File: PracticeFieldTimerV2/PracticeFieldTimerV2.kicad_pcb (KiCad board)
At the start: 2 copper layers, 103 x 96 mm, 36 parts, among them J1 External Controls, J2 Screw_Terminal_01x04, J3 Panel, J5 /CAN Enable, J6 RJ45-B, J7 RJ45-A, U1 ESP32-DevKitC, U4 DS3231MZ_TRL, U5 SN65HVD230DR

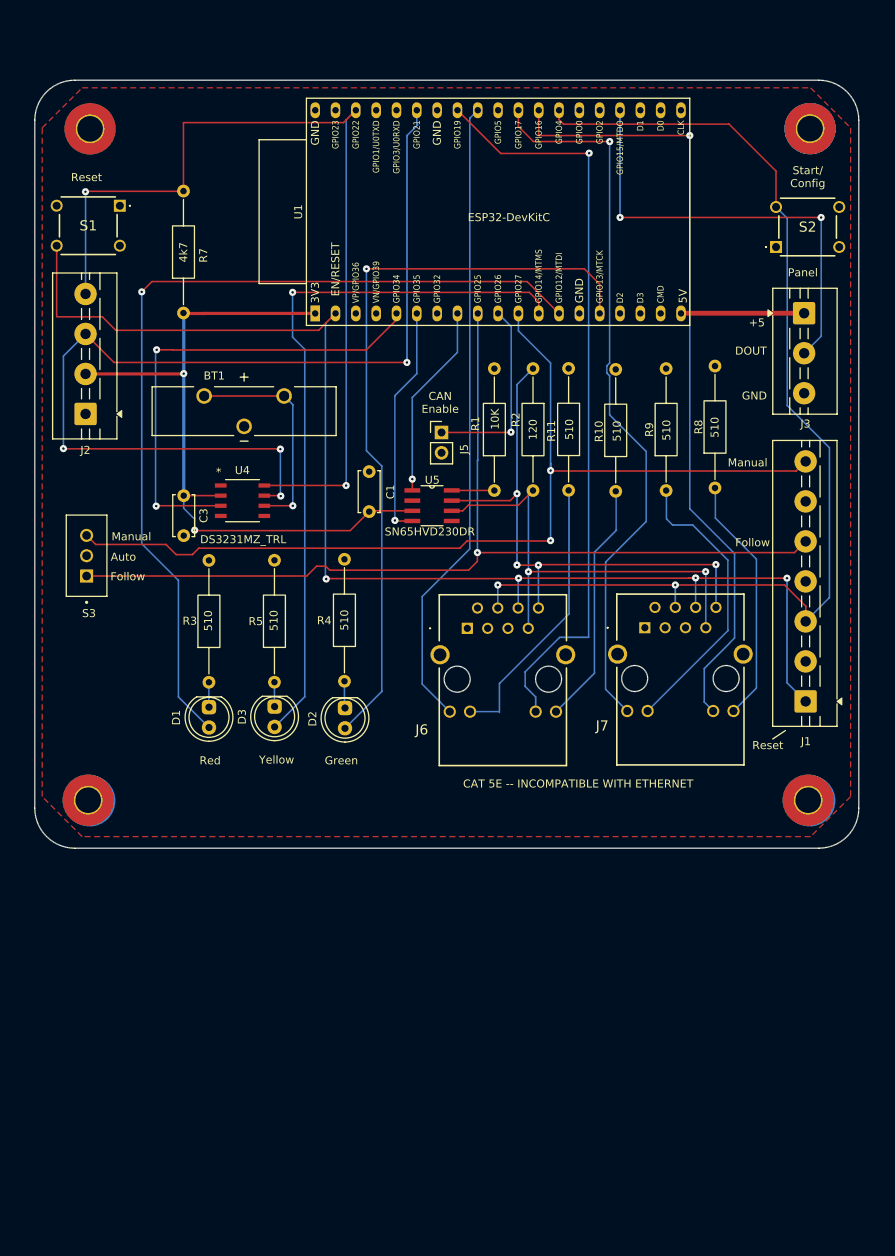
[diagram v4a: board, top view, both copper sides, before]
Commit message: Add missing resistors. Fix the warnings we can. Cosmetic fixes. Getting close
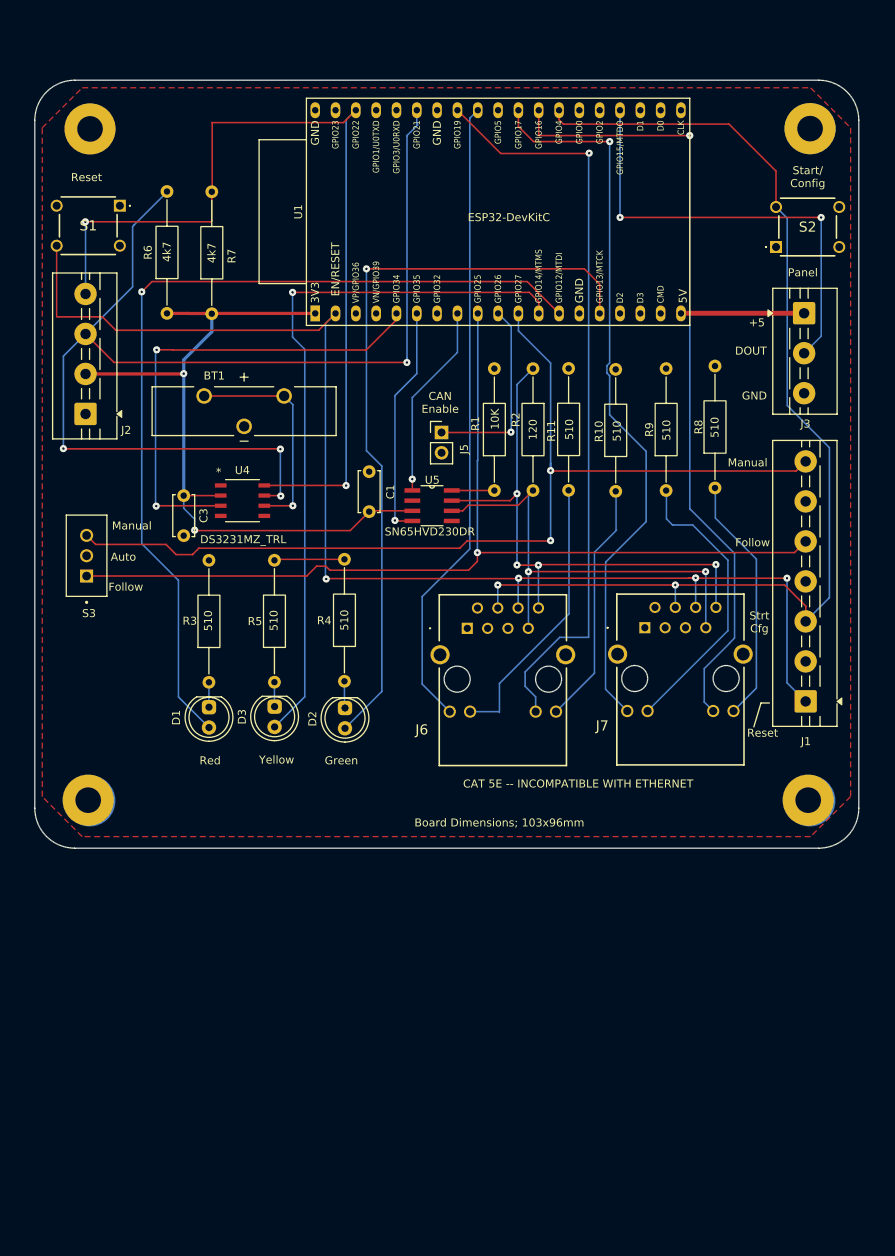
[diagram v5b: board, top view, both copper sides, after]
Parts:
- added R6: 4k7, Resistor_THT:R_Axial_DIN0207_L6.3mm_D2.5mm_P15.24mm_Horizontal, F.Cu at (57.0, 60.1)
- moved R7 3.54 mm to (62.6, 60.2)
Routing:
- net I2C SDA: track 124.4 -> 146.3 mm
- net GND: track 0.92 -> 9.72 mm
- net +3.3V: track 89.3 -> 92.7 mm
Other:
- board text added: "Board Dimensions; 103x96mm"
- board text added: "Strt Cfg"

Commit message: Smush components closer together to reduce width under 100 mm because cost of manufacture. Tidied up a bit. Added missing labels. In short: mucked about.
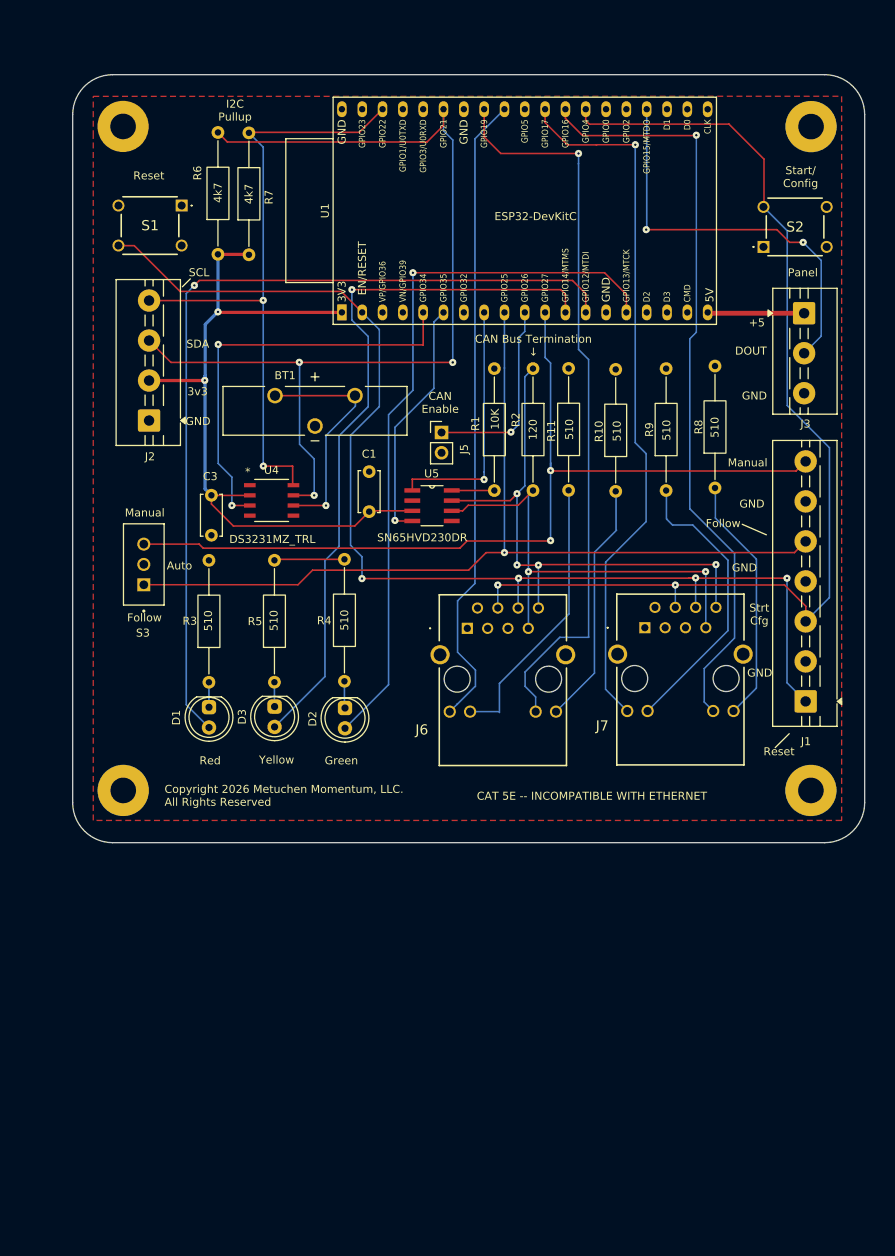
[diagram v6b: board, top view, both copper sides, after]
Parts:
- moved R6 9.75 mm to (63.4, 52.8)
- moved BT1 8.86 mm to (75.5, 72.3)
- moved R7 8.71 mm to (67.3, 52.8)
- moved J2 7.98 mm to (54.8, 73.5)
- moved S1 7.72 mm to (58.9, 46.7)
- moved S3 7.23 mm to (54.1, 91.5)
- moved REF** 4.55 mm to (51.6, 119.8)
- moved ? 4.37 mm to (51.6, 119.8)
- moved REF** 4.14 mm to (51.6, 36.8)
- moved U4 3.64 mm to (70.1, 83.5)
- moved C3 3.46 mm to (62.6, 82.9)
- moved U1 3.34 mm to (78.9, 60.0)
- moved S2 1.57 mm to (131.6, 51.8)
- moved ? 1.30 mm to (137.5, 119.8)
- moved REF** 1.27 mm to (137.5, 119.8)
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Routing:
- net I2C SCL: track 113.4 -> 80.5 mm
- net I2C SDA: track 146.3 -> 122.8 mm, vias 4 -> 3
- net /RST: track 161.3 -> 148.5 mm
- net /Manual: track 122.7 -> 113.1 mm
- net /Follow: track 122.6 -> 115.0 mm
- net CAN TX: track 24.5 -> 31.3 mm
- net SQW: track 59.3 -> 52.8 mm
- net Panel DOUT: track 56.4 -> 51.0 mm
- net +5V: track 15.4 -> 12.0 mm
- net /RJ45-A-Green: track 98.4 -> 95.1 mm
- net Net-(D2-A): track 93.8 -> 90.5 mm
- net Net-(D1-A): track 112.3 -> 109.1 mm
- net /CFG-START: track 138.4 -> 135.2 mm
- net +3.3V: track 92.7 -> 89.8 mm
- net /RJ45-B-Green: track 94.5 -> 92.4 mm
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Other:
- board size 103 x 96 mm -> 99 x 96 mm
- board text added: "3v3"
- board text added: "Board Dimensions; 99x96mm"
- board text added: "CAN Bus Termination ↓"
- board text added: "Copyright 2026 Metuchen Momentum, LLC. All Rights Reserved"
- board text added: "I2C Pullup"
- board text added: "SCL"
- board text added: "SDA"
- board text added: "← 83mm → center to center"
- board text added: "← 86mm center to center →"
- board text removed: "Board Dimensions; 103x96mm"
- board text removed: "← 84mm → center to center"
- board text removed: "← 90mm center to center →"
